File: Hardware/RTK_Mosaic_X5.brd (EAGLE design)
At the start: 151.8 x 101.6 mm, 299 parts, among them J2 MAGJACK-POE, J3 MICRO-SD-PUSH-PUSH-EXT-PIN, J4 Vertical Qwiic Connector, J9 MAGJACK-POE, U1 ESP32-WROVER-IE, U10 POE_PSU-DP990X, U17 URB2405YMD, U2 CH340C, U3 XC6222B331MR-G, U4 TXS0108, U5 TXS0108, U6 XC6222B331MR-G

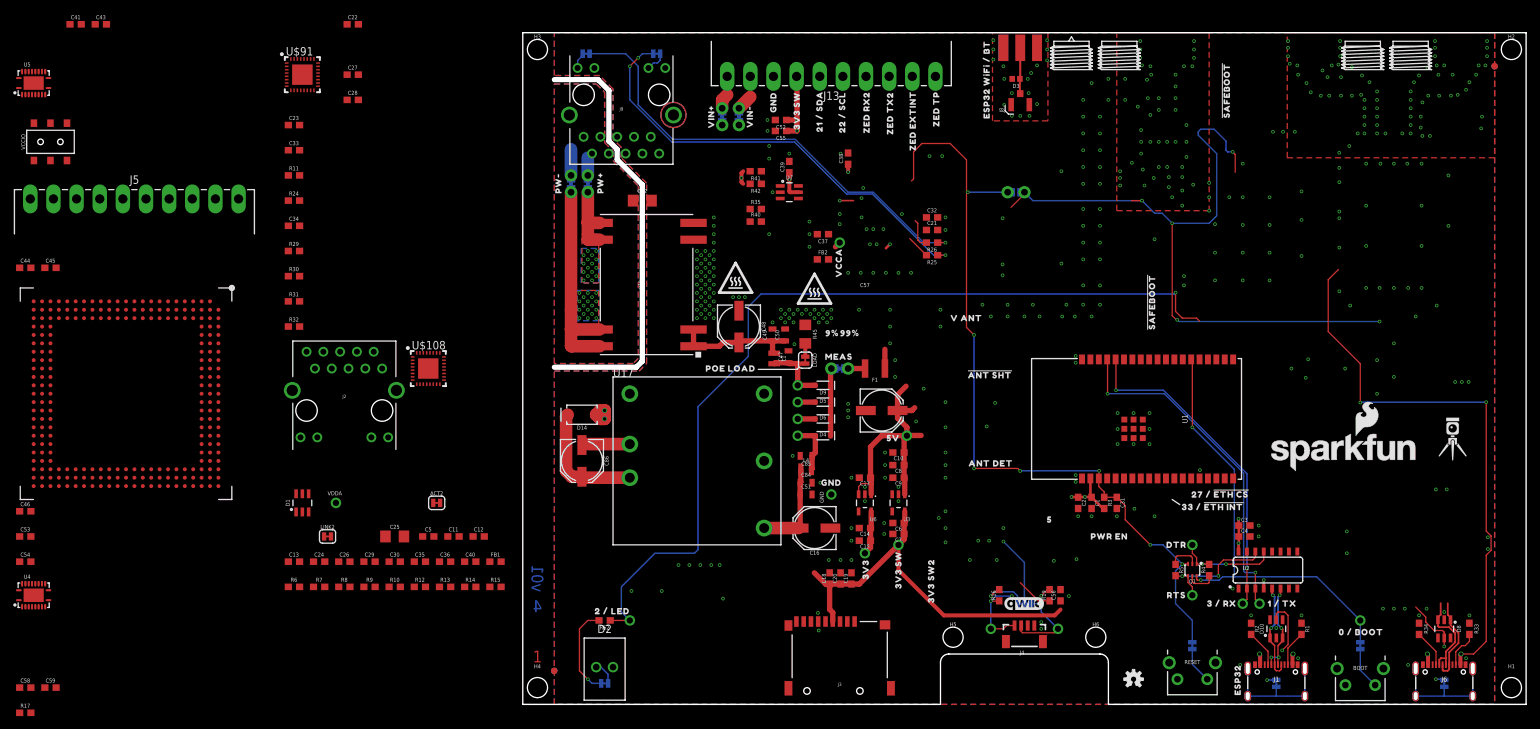
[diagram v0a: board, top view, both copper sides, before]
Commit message: Ready for airwire review
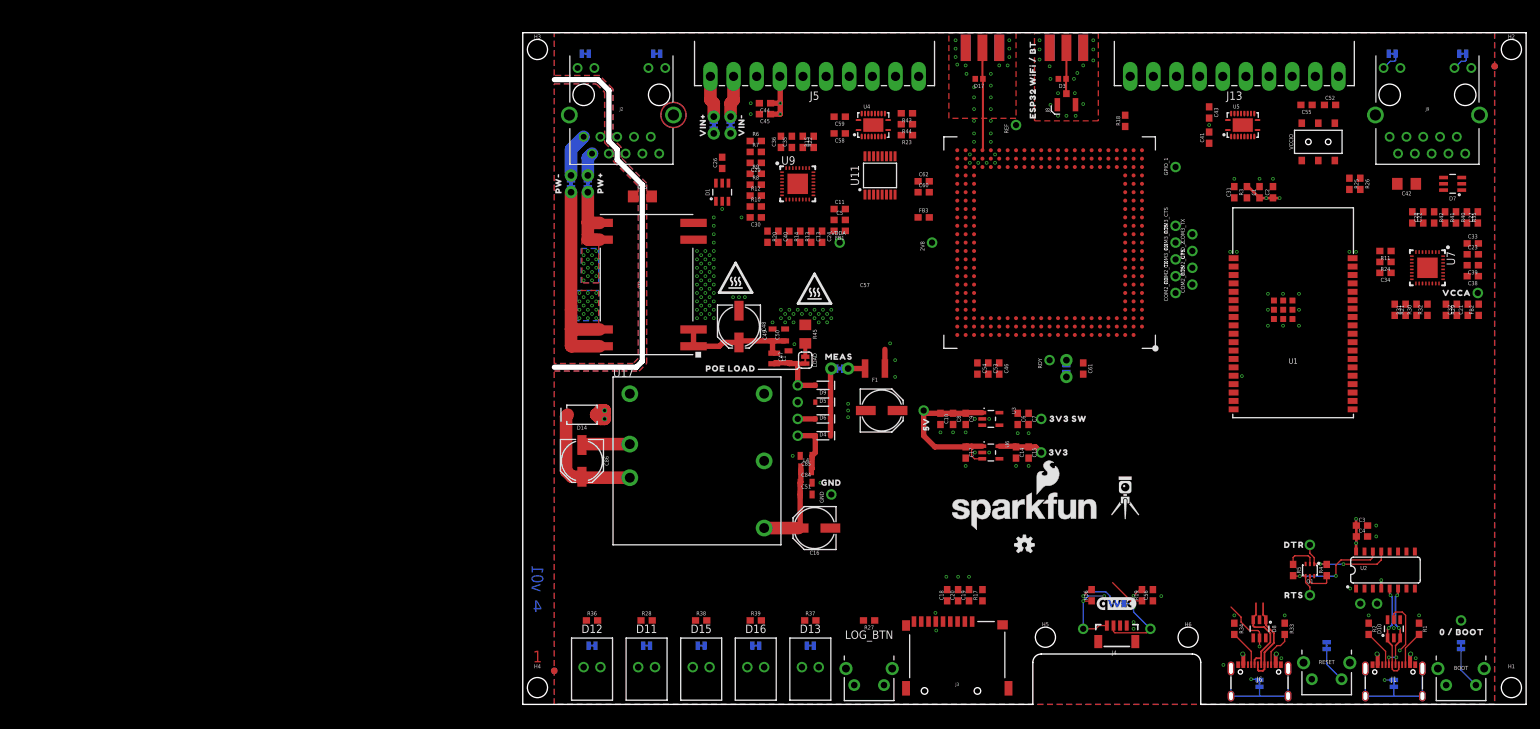
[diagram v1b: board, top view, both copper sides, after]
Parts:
- removed C12, C37: 0.1uF, SparkFun-Capacitors:0603
- removed D2: LED-RIGHT-ANGLE-PTH-GREEN, SparkFun-LED:CBI-RIGHT-ANGLE-PTH
- removed GNSS_RESET: JUMPER-COMBO_2_NO, SparkFun-Jumpers:COMBO-JUMPER_2_NO
- removed LED: JUMPER-SMT_2_NC_TRACE_SILK, SparkFun-Jumpers:SMT-JUMPER_2_NC_TRACE_SILK
- removed R62: 470, SparkFun-Resistors:0603
- removed TP_LED: TEST-POINTPOGO_PTH, SparkFun-Connectors:1X01_NO_SILK
- removed U$100, U$35: (no value), output:3_#_RX20
- removed U$101: (no value), output:19_#_POCI19
- removed U$102: (no value), output:18_#_SCK6
- removed U$104, U$47: (no value), output:99#2230
- removed U$105, U$49: (no value), output:V_ANT2229
- removed U$106, U$44: (no value), output:9#2230
- removed U$108, U$91: KSZ8041NL, Septentrio_Mosaic:MLF55Q-32LD
- removed U$109, U$27: (no value), output:33_#_#ETH_INT#0
- removed U$11: (no value), output:ZED_TX1
- removed U$111, U$29: (no value), output:27_#_#ETH_CS#0
- removed U$12, U$41, U$8, U$93: (no value), output:#SAFEBOOT#2226
- removed U$13: (no value), output:ZED_RX0
- removed U$14: (no value), output:NEO_TX2
- removed U$141, U$80: (no value), output:PWR_EN2233
- removed U$15: (no value), output:NEO_RX3
- removed U$154: (no value), output:#GNSS_RESET#0
- removed U$16: (no value), output:GND2
- removed U$17, U$65: (no value), output:3V3_SW20
- removed U$19: (no value), output:12_#_SDA20
- removed U$20: (no value), output:15_#_SCL213
- removed U$22, U$23: (no value), output:3V3_SW3
- removed U$25, U$26: (no value), output:21_#_SDA4
- removed U$28, U$30: (no value), output:22_#_SCL22
- removed U$31, U$32: (no value), output:ZED_RX223
- removed U$33, U$36: (no value), output:ZED_TX2224
- removed U$34, U$99: (no value), output:1_#_TX20
- removed U$37, U$38: (no value), output:ZED_EXTINT2225
- removed U$39, U$40: (no value), output:ZED_TP2226
- removed U$42, U$94: (no value), output:ANT_DET2227
- removed U$43, U$95: (no value), output:#ANT_SHT#2228
- removed U$48: (no value), output:#I�C#0
- removed U$57, U$66: (no value), output:2_#_LED0
- removed U$58: (no value), output:#LED#2234
- removed U$64: (no value), output:36_#_SD_DET0
- removed U$67: (no value), output:#PMODE0#0
- removed U$68: (no value), output:#PMODE1#1
- removed U$69: (no value), output:#PMODE2#2
- removed U$73, U$75: (no value), output:50
- removed U$78: (no value), output:ESP320
- removed U$79: (no value), output:UART14
- removed U$89: (no value), output:4_#_#SD_CS#15
- removed U$98: (no value), output:23_#_PICO23
- added 2V8, COM2_CTS, COM2_RTS, COM2_RX, COM2_TX, COM3_CTS, COM3_RTS, COM3_RX, COM3_TX, GPIO_1, GPIO_2, RDY, REF: TEST-POINTPOGO_PTH, SparkFun-Connectors:1X01_NO_SILK
- added BT, LOG, PVT, RTK, WIFI: JUMPER-SMT_2_NC_TRACE_SILK, SparkFun-Jumpers:SMT-JUMPER_2_NC_TRACE_SILK
- added C60, C61: 2.2uF, SparkFun-Capacitors:0603
- added C62: 0.1uF, SparkFun-Capacitors:0603
- added D11: LED-RIGHT-ANGLE-PTH-AMBER, SparkFun-LED:CBI-RIGHT-ANGLE-PTH
- added D12, D15, D16: LED-RIGHT-ANGLE-PTH-BLUE, SparkFun-LED:CBI-RIGHT-ANGLE-PTH
- added D13: LED-RIGHT-ANGLE-PTH-GREEN, SparkFun-LED:CBI-RIGHT-ANGLE-PTH
- added D17: PESD0402, SparkFun-DiscreteSemi:0402
- added FB3: 470Ω, SparkFun-Coils:0603
- added LOG_BTN: MOMENTARY-SWITCH-SPST-PTH-RIGHT-ANGLE-8-020, SparkFun-Switches:TACTILE_SWITCH_PTH_RA_8-020
- added MOSAIC_RF: ANTENNA-SMA-GROUNDEDEDGE_SMA, SparkFun-RF:SMA-EDGE
- added MOSAIC_RST: JUMPER-COMBO_2_NO, SparkFun-Jumpers:COMBO-JUMPER_2_NO
- added R18, R22, R23, R43, R44: 10k, SparkFun-Resistors:0603
- added R20, R21: 4.7k, SparkFun-Resistors:0603
- added R27, R28, R36, R37, R38, R39: 1k, SparkFun-Resistors:0603
- added U11: SN74AVC4T774PW, SparkFun-IC-Comms:SOP65P640X120-16N
- added U7, U9: KSZ8041NL, Septentrio_Mosaic:MLF55Q-32LD
- added U8: MOSAIC-X5X5, Septentrio_Mosaic:MOSAIC_LGA
- U$2: value MOSAIC-X5X5 -> (none); device Septentrio_Mosaic:MOSAIC_LGA -> output:#ACT#0
- U$4: device output:#I�C#0 -> output:#LINK#1
- moved VCCIO 191.8 mm to (120.7, 85.1)
- moved U5 183.0 mm to (109.2, 87.6)
- moved C23 179.4 mm to (144.0, 68.1)
- moved C33 178.9 mm to (144.0, 69.7)
- moved R29 174.5 mm to (140.0, 59.7), turned to 270 degrees
- moved C41 172.3 mm to (104.1, 85.7), turned to 90 degrees
- moved C27 171.5 mm to (144.8, 73.7), turned to 90 degrees
- moved R32 171.5 mm to (137.2, 59.7), turned to 90 degrees
- moved R30 169.9 mm to (135.5, 59.7), turned to 90 degrees
- moved C43 168.2 mm to (104.1, 89.5), turned to 270 degrees
- moved R31 168.2 mm to (133.9, 59.7), turned to 90 degrees
- moved R11 165.5 mm to (130.8, 68.6), turned to 180 degrees
- moved R24 165.4 mm to (130.8, 66.9), turned to 180 degrees
- moved C34 165.3 mm to (130.8, 65.3), turned to 180 degrees
- moved C22 162.9 mm to (134.9, 73.7), turned to 270 degrees
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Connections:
- removed net ESP2/LED: R62.1, TP_LED.1
- removed net GNSS_!RESET!: GNSS_RESET.1, GNSS_RESET.3
- removed net N$45: D2.A, LED.1
- removed net N$7: LED.2, R62.2
- removed net SD_DAT0: J3.7
- new net 1.8V: C60.1, C62.1, R18.2, U11.16, U11.6, U11.7, U11.8, U8.AC4
- new net 2V8: 2V8.1, U8.M23, U8.N23
- new net COM2_CTS: COM2_CTS.1, U8.J1
- new net COM2_RTS: COM2_RTS.1, U8.G1
- new net COM2_RX: COM2_RX.1, U8.F1
- new net COM2_TX: COM2_TX.1, U8.H1
- new net COM3_CTS: COM3_CTS.1, U8.N1
- new net COM3_RTS: COM3_RTS.1, U8.L1
- new net COM3_RX: COM3_RX.1, U8.K1
- new net COM3_TX: COM3_TX.1, U8.M1
- new net GPIO_1: GPIO_1.1, U8.AA4
- new net GPIO_2: GPIO_2.1, U8.L3
- new net LED_PVT: R38.1, U8.A14
- new net LED_RTK: R39.1, U8.M3
- new net LOG_LED: R37.1, U8.B2
- new net MOSAIC_!RST!: MOSAIC_RST.1, MOSAIC_RST.3, U8.A11
- new net MOSAIC_EVENTA_1V8: U11.3, U8.AC6
- new net MOSAIC_EVENTB_1V8: U11.4, U8.AC7
- new net MOSAIC_PPSO_1V8: U11.5, U8.AC8
- new net MOSAIC_RF: D17.1, MOSAIC_RF.SIG, U8.AC20
- new net N$11: LOG_BTN.2, R27.1
- new net N$16: LOG.2, R37.2
- new net N$17: D13.A, LOG.1
- new net N$18: D11.A, WIFI.1
- new net N$22: BT.1, D12.A
- new net N$26: BT.2, R36.2
- new net N$32: R28.2, WIFI.2
- new net N$35: D15.A, PVT.1
- new net N$36: D16.A, RTK.1
- new net N$37: R39.2, RTK.2
- new net N$38: PVT.2, R38.2
- new net N$6: FB3.2, U8.P23, U8.R23
- new net N$9: R18.1, U8.AC3
- new net RDY: RDY.1, U8.A12
- new net REF: REF.1, U8.AC16, U8.AC17
- net !RESET!: now also MOSAIC_RST.2, MOSAIC_RST.4; no longer GNSS_RESET.2, GNSS_RESET.4
- net 3.3V: now also R21.2, U7.17; no longer U$91.17
- net 3.3V_SW: now also R20.2, U11.15, U8.A18, U8.A19, U8.A20, U8.B18, U8.B19, U8.B20, U8.B8, U8.C18, U8.C19, U8.C20, U9.17; no longer U$108.17, U$2.A18, U$2.A19, U$2.A20, U$2.B18, U$2.B19, U$2.B20, U$2.B8, U$2.C18, U$2.C19, U$2.C20
- net 5V: now also C61.1, FB3.1, U8.A8; no longer U$2.A8, U$2.P23, U$2.R23
- net ACT_ESP32: now also U7.31; no longer U$91.31
- net ACT_MOSAIC: now also U9.31; no longer U$108.31
- net D+_MOSAIC: now also U8.A5; no longer U$2.A5
- net D-_MOSAIC: now also U8.A6; no longer U$2.A6
- net ESP0/!BOOT!: now also U7.9; no longer U$91.9
- net ESP12_LED_WIFI: now also R28.1
- net ESP15_LED_BT: now also R36.1
- net ESP18_MDIO: now also R21.1, U7.11; no longer U$91.11
- net ESP19_TXD0: now also U7.24; no longer U$91.24
- net ESP21_TXEN: now also U7.23; no longer U$91.23
- net ESP22_TXD1: now also U7.25; no longer U$91.25
- net ESP23_MDC: now also U7.12; no longer U$91.12
- net ESP2_COM4_RX: now also U8.D3; no longer U$2.D3
- net ESP32_TX: now also U5.3; no longer U5.1
- net ESP32_TX_IO: now also U5.18; no longer U5.20
- net ESP33_RTS: now also U5.4; no longer U5.3
- net ESP33_RTS_IO: now also U5.17; no longer U5.18
- net ESP34_RX: now also U5.1; no longer U5.4
- net ESP34_RX_IO: now also U5.20; no longer U5.17
- net ESP4_COM4_TX: now also U8.E3; no longer U$2.E3
- net ESP5_ERST: now also U7.32; no longer U$91.32
- net ETHER_!RST!: now also R22.2, U8.F2, U9.32; no longer U$2.F2
- net ETHER_CLK: now also U8.AA2, U9.9; no longer U$108.9, U$2.AA2
- net ETHER_CRSDV: now also U8.N2, U9.18; no longer U$108.18, U$2.N2
- net ETHER_MDC: now also U8.V2, U9.12; no longer U$108.12, U$2.V2
- net ETHER_MDIO: now also R20.1, U8.W2, U9.11; no longer U$108.11, U$2.W2
- net ETHER_RXD0: now also U8.R2, U9.16; no longer U$108.16, U$2.R2
- net ETHER_RXD1: now also U8.T2, U9.15; no longer U$108.15, U$2.T2
- net ETHER_RXER: now also U8.M2, U9.20; no longer U$108.20, U$2.M2
- net ETHER_TXD0: now also U8.J2, U9.24; no longer U$108.24, U$2.J2
- net ETHER_TXD1: now also U8.H2, U9.25; no longer U$108.25, U$2.H2
- net ETHER_TXEN: now also U8.L2, U9.23; no longer U$108.23, U$2.L2
- net GND: now also C60.2, C61.2, C62.2, D11.C, D12.C, D13.C, D15.C, D16.C, D17.2, LOG_BTN.1, MOSAIC_RF.GND@0, MOSAIC_RF.GND@1, MOSAIC_RF.GND@2, MOSAIC_RF.GND@3, R22.1, R43.1, R44.1, U11.1, U11.10, U11.2, U11.9, U7.1, U7.GND, U8.A15, U8.A16, U8.A17, U8.A21, U8.A22, U8.A23, U8.A3, U8.A4, U8.A7, U8.AA13, U8.AA14, U8.AA15, U8.AA16, U8.AA17, U8.AA18, U8.AA19, U8.AA20, U8.AA21, U8.AA22, U8.AA23, U8.AB13, U8.AB14, U8.AB15, U8.AB16, U8.AB17, U8.AB18, U8.AB19, U8.AB2, U8.AB20, U8.AB21, U8.AB22, U8.AB23, U8.AB3, U8.AB4, U8.AB5, U8.AB6, U8.AB7, U8.AB8, U8.AC13, U8.AC15, U8.AC18, U8.AC19, U8.AC21, U8.AC22, U8.AC23, U8.B13, U8.B17, U8.B21, U8.B4, U8.B5, U8.B6, U8.B7, U8.C15, U8.C16, U8.C17, U8.C23, U8.C4, U8.C7, U8.D2, U8.D21, U8.D22, U8.D23, U8.E2, U8.E21, U8.E22, U8.E23, U8.F21, U8.F22, U8.F23, U8.G2, U8.G21, U8.G23, U8.H21, U8.H22, U8.H23, U8.J21, U8.J22, U8.J23, U8.K2, U8.K21, U8.K22, U8.K23, U8.L21, U8.L22, U8.L23, U8.M21, U8.M22, U8.N21, U8.N22, U8.P1, U8.P2, U8.P21, U8.P22, U8.P3, U8.R21, U8.R22, U8.R3, U8.T21, U8.T22, U8.T23, U8.U2, U8.U21, U8.U22, U8.U23, U8.V21, U8.V22, U8.V23, U8.W21, U8.W22, U8.W23, U8.Y2, U8.Y21, U8.Y22, U8.Y23, U9.1, U9.GND; no longer C12.2, C37.2, D2.C, U$108.1, U$108.GND, U$2.A15, U$2.A16, U$2.A17, U$2.A21, U$2.A22, U$2.A23, U$2.A4, U$2.A7, U$2.AA13, U$2.AA14, U$2.AA15, U$2.AA16, U$2.AA17, U$2.AA18, U$2.AA19, U$2.AA20, U$2.AA21, U$2.AA22, U$2.AA23, U$2.AB13, U$2.AB14, U$2.AB15, U$2.AB16, U$2.AB17, U$2.AB18, U$2.AB19, U$2.AB2, U$2.AB20, U$2.AB21, U$2.AB22, U$2.AB23, U$2.AB3, U$2.AB4, U$2.AB5, U$2.AB6, U$2.AB7, U$2.AB8, U$2.AC13, U$2.AC15, U$2.AC18, U$2.AC19, U$2.AC21, U$2.AC22, U$2.AC23, U$2.B13, U$2.B17, U$2.B21, U$2.B4, U$2.B5, U$2.B6, U$2.B7, U$2.C15, U$2.C16, U$2.C17, U$2.C23, U$2.C4, U$2.C7, U$2.D2, U$2.D21, U$2.D22, U$2.D23, U$2.E2, U$2.E21, U$2.E22, U$2.E23, U$2.F21, U$2.F22, U$2.F23, U$2.G2, U$2.G21, U$2.G23, U$2.H21, U$2.H22, U$2.H23, U$2.J21, U$2.J22, U$2.J23, U$2.K2, U$2.K21, U$2.K22, U$2.K23, U$2.L21, U$2.L22, U$2.L23, U$2.M21, U$2.M22, U$2.N21, U$2.N22, U$2.P1, U$2.P2, U$2.P21, U$2.P22, U$2.P3, U$2.R21, U$2.R22, U$2.R3, U$2.T21, U$2.T22, U$2.T23, U$2.U2, U$2.U21, U$2.U22, U$2.U23, U$2.V21, U$2.V22, U$2.W21, U$2.W22, U$2.W23, U$2.Y2, U$2.Y21, U$2.Y22, U$2.Y23, U$91.1, U$91.GND
- net LINK_ESP32: now also U7.30; no longer U$91.30
- net LINK_MOSAIC: now also U9.30; no longer U$108.30
- net MOSAIC_CTS: now also U8.E1; no longer U$2.E1
- net MOSAIC_EVENTA: now also U11.14; no longer U$2.AC6
- net MOSAIC_EVENTA_IO: now also R43.2
- net MOSAIC_EVENTB: now also U11.13; no longer U$2.AC7
- net MOSAIC_EVENTB_IO: now also R44.2
- net MOSAIC_LOG_BTN: now also U8.K3; no longer U$2.K3
- net MOSAIC_LOG_BTN_IO: now also R23.2, R27.2
- net MOSAIC_PPSO: now also U11.12; no longer U$2.AC8
- net MOSAIC_RTS: now also U8.C1; no longer U$2.C1
- net MOSAIC_RX: now also U8.B1; no longer U$2.B1
- net MOSAIC_TX: now also U8.D1; no longer U$2.D1
- net N$146: now also U9.2; no longer U$108.2
- net N$147: now also U9.10; no longer U$108.10
- net N$148: now also U9.28; no longer U$108.28
- net N$23: now also U7.2; no longer U$91.2
- net N$24: now also U7.10; no longer U$91.10
- net N$25: now also U7.28; no longer U$91.28
- net N$30: now also U7.16; no longer U$91.16
- net N$31: now also U7.15; no longer U$91.15
- net N$39: now also U7.18; no longer U$91.18
- net RD+_ESP32: now also U7.5; no longer U$91.5
- net RD+_MOSAIC: now also D1.1, U9.5; no longer D1.4, U$108.5
- net RD-_ESP32: now also D7.6, U7.4; no longer D7.3, U$91.4
- net RD-_MOSAIC: now also U9.4; no longer U$108.4
- net SD_CLK: now also U8.AA1; no longer U$2.AA1
- net SD_CMD: now also U8.AB1; no longer U$2.AB1
- net SD_DATA: now also J3.7, U8.Y1; no longer U$2.Y1
- net TD+_ESP32: now also D7.3, U7.7; no longer D7.6, U$91.7
- net TD+_MOSAIC: now also U9.7; no longer U$108.7
- net TD-_ESP32: now also U7.6; no longer U$91.6
- net TD-_MOSAIC: now also D1.4, U9.6; no longer D1.1, U$108.6
- net VCCA: now also U7.3; no longer C37.1, U$91.3
- net VCCIO: now also R23.1
- net VDDA: now also U9.3; no longer C12.1, U$108.3
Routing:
- net V_USB_2: track 240.5 -> 23.0 mm, vias 5 -> 3
- net ESP2/LED: track 135.0 -> 0.00 mm, vias 1 -> 0
- net !RESET!: track 123.0 -> 0.00 mm, vias 7 -> 0
- net V_USB: track 141.6 -> 21.6 mm
- net GNSS_!RESET!: track 107.4 -> 0.00 mm, vias 5 -> 0
- net 3.3V: track 108.2 -> 31.5 mm, vias 10 -> 5
- net N$12: track 70.3 -> 0.00 mm, vias 1 -> 0
- net N$21: track 68.1 -> 0.00 mm, vias 3 -> 0
- net ESP0/!BOOT!: track 67.1 -> 0.00 mm, vias 2 -> 0
- net 3.3V_SW: track 58.7 -> 0.00 mm
- net CH340-RXI: track 52.4 -> 0.00 mm, vias 2 -> 0
- net CH340-TXO: track 49.6 -> 0.00 mm, vias 2 -> 0
- net VCCA: track 49.5 -> 0.00 mm, vias 10 -> 0
- net MOSAIC_RF: track 0.00 -> 15.6 mm
- net N$7: track 13.9 -> 0.00 mm, vias 1 -> 0
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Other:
- outline, holes or cut-outs redrawn
- board text added: "Controlled Impedance: JLC7628 Material: TG155 4-Layers Thickness: 1.6mm Outer Copper: 1oz Inner Copper: 0.5oz Finish: ENIG Red Solder Resist White Silkscreen No clean process"
- board text removed: "Controlled Impedance: JLC7628 Material: TG155 4-Layers Thickness: 1.6mm Outer Copper: 1oz Inner Copper: 0.5oz Finish: HASL Lead Free Red Solder Resist White Silkscreen"

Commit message: Silk added. Layer 15 polygon is now GND.
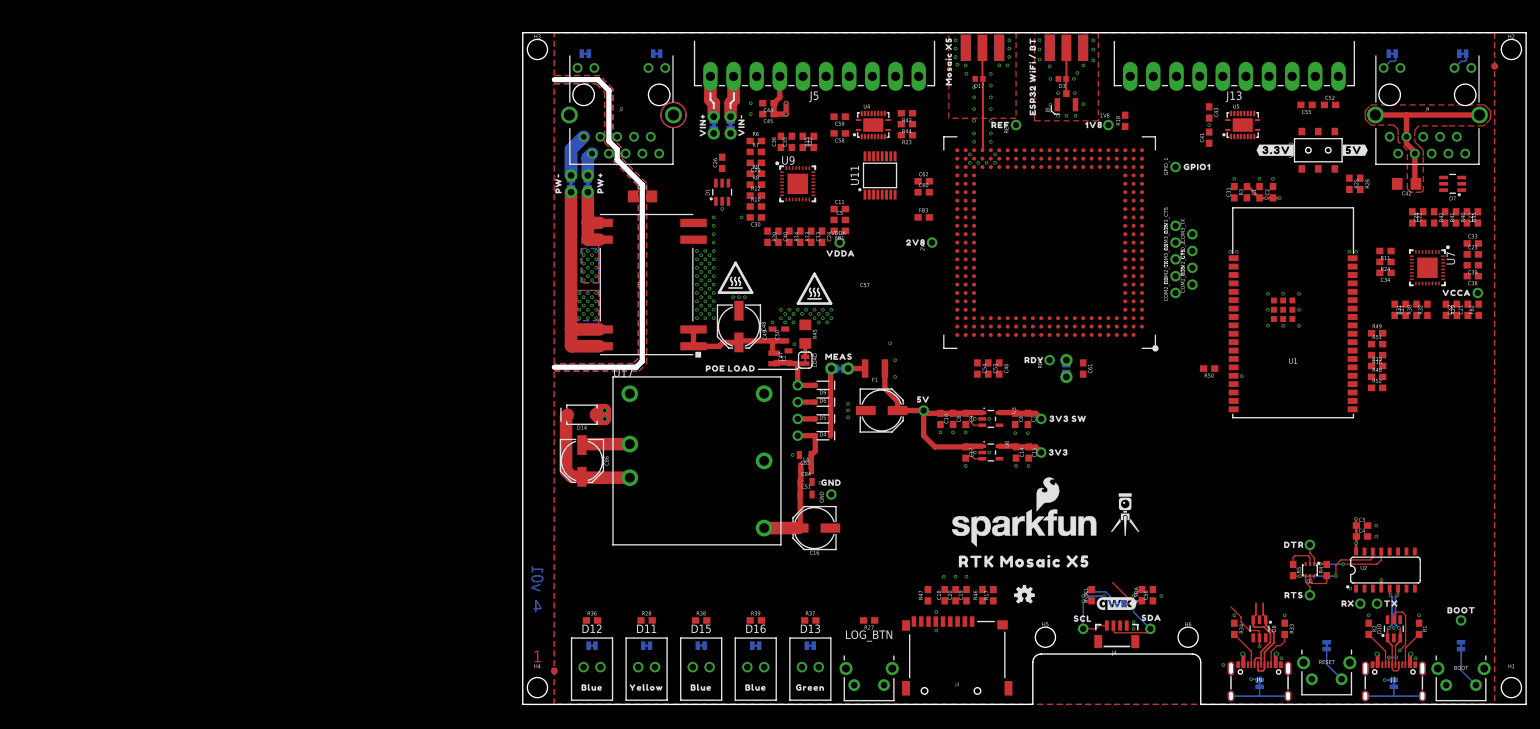
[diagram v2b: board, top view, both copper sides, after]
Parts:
- removed U$148: (no value), output:RESET0
- removed U$149: (no value), output:0_#_BOOT0
- added 1V8: TEST-POINTPOGO_PTH, SparkFun-Connectors:1X01_NO_SILK
- added R46, R47, R48, R49, R50: 10k, SparkFun-Resistors:0603
- added R51, R52: 0, SparkFun-Resistors:0603
- added R_SCL, R_SDA: 2.2k, SparkFun-Resistors:0603
- added U$100: (no value), output:MOSAIC_X50
- added U$101, U$102: (no value), output:1V80
- added U$103, U$105, U$106: (no value), output:BLUE0
- added U$104: (no value), output:YELLOW1
- added U$108: (no value), output:GREEN2
- added U$11: (no value), output:#LOG#4
- added U$12: (no value), output:#PVT#2
- added U$13: (no value), output:#RTK#3
- added U$14: (no value), output:#WIFI#1
- added U$15: (no value), output:#BOOT#6
- added U$16: (no value), output:#_______________MOSAIC_X5_______________#8
- added U$17, U$31: (no value), output:#RX#2
- added U$19, U$29: (no value), output:#RTS#4
- added U$20, U$30: (no value), output:#CTS#5
- added U$22: (no value), output:#EVENT_A#6
- added U$23: (no value), output:#EVENT_B#7
- added U$25, U$28: (no value), output:#GND#0
- added U$26, U$27: (no value), output:#VCCIO#1
- added U$32: (no value), output:#TX#3
- added U$33: (no value), output:#PPSO#11
- added U$34: (no value), output:#LOG_BTN#33
- added U$35: (no value), output:#SCL#10
- added U$36: (no value), output:#SDA#9
- added U$37: (no value), output:#MOSAIC#8
- added U$38: (no value), output:#___________________ESP32___________________#34
- added U$39: (no value), output:#3#3V#6
- added U$40: (no value), output:#5V#0
- added U$41, U$42: (no value), output:2V8220
- added U$43, U$44: (no value), output:BOOT2
- added U$47: (no value), output:COM2_CTS219
- added U$48: (no value), output:COM2_RTS219
- added U$49: (no value), output:COM2_RX219
- added U$54: (no value), output:COM2_TX219
- added U$57: (no value), output:COM3_CTS18
- added U$58: (no value), output:COM3_RTS18
- added U$64: (no value), output:COM3_RX219
- added U$65: (no value), output:COM3_TX18
- added U$66, U$67: (no value), output:GPIO17
- added U$68: (no value), output:GPIO218
- added U$69, U$99: (no value), output:RTK_MOSAIC_X50
- added U$73: (no value), output:MOSAIC_#RST#6
- added U$75, U$78: (no value), output:RDY5
- added U$79, U$80: (no value), output:REF219
- added U$8: (no value), output:#BT#0
- added U$89, U$90: (no value), output:RX0
- added U$91, U$92: (no value), output:SCL3
- added U$93, U$94: (no value), output:SDA4
- added U$95, U$96: (no value), output:TX1
- added U$97, U$98: (no value), output:VDDA220
- R16: value 2.2k -> 10k
- R19: value 2.2k -> 1k
- U$18: device output:GND2 -> output:#TX#3
- U$7: device output:0_#_BOOT0 -> output:##RESET##5
- moved R16 56.4 mm to (129.5, 52.8), turned to 180 degrees
- moved R19 49.7 mm to (129.5, 51.2), turned to 0 degrees
- moved U$7 19.8 mm to (122.7, 8.89), flipped to the bottom
- moved U$18 10.8 mm to (46.4, 89.3)
- moved LOGO4 7.62 mm to (76.2, 16.5)
- moved U$86 5.90 mm to (59.1, 46.1), turned to 0 degrees
- moved U$153 3.81 mm to (61.0, 27.6)
- moved D5 2.54 mm to (45.7, 43.2)
- moved D6 2.54 mm to (45.7, 45.7)
- moved LOGO5 2.54 mm to (76.2, 26.7)
- moved LOGO6 2.54 mm to (79.8, 31.8)
- moved LOGO7 2.54 mm to (76.2, 26.7)
- moved LOGO8 2.54 mm to (72.6, 31.8)
- moved U$152 2.54 mm to (91.4, 28.7)
- moved U$82 2.54 mm to (42.2, 43.2)
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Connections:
- net N$3 renamed SD_DAT3
- removed net ESP0/!BOOT!: BOOT_SW.1, Q1.6, TP_BOOT.1, U1.25, U7.9
- removed net ESP2_COM4_RX: U1.24, U8.D3
- removed net ESP4_COM4_TX: U1.26, U8.E3
- new net !BOOT!: BOOT_SW.1, Q1.6, R16.1, R19.2, TP_BOOT.1
- new net COM4_RX: R52.2, U8.D3
- new net COM4_TX: R51.2, U8.E3
- new net ESP2_TX: R48.1, R52.1, U1.24
- new net ESP4_RX: R51.1, U1.26
- new net ESP_REFCLK: R19.1, U1.25, U7.9
- net 1.8V: now also 1V8.1
- net 3.3V: now also R16.2, R49.2
- net 3.3V_SW: now also R22.1, R46.2, R47.2
- net ESP12_LED_WIFI: now also R50.1
- net ESP14_SCL: now also R_SCL.1; no longer R16.1
- net ESP15_SDA: now also R_SDA.1; no longer R19.1
- net ESP5_ERST: now also R49.1
- net GND: now also R48.2, R50.2; no longer R22.1
- net N$14: now also R_SCL.2; no longer R16.2
- net N$15: now also R_SDA.2; no longer R19.2
- net SD_CMD: now also R46.1
- net SD_DATA: now also R47.1
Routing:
- net GND-ISO: track 0.00 -> 26.7 mm
- net 5V: track 28.7 -> 40.2 mm
- net 3.3V_SW: track 0.00 -> 6.71 mm
- net V_USB: track 21.6 -> 24.3 mm
- net VCCIO: track 8.64 -> 9.56 mm
- removed copper zone on layer 15, net 3.3V_SW

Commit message: Routed
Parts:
- moved R26 8.03 mm to (133.2, 73.7)
- moved R25 8.03 mm to (131.6, 73.7)
- moved C5 3.81 mm to (48.3, 77.1)
- moved U$152 3.81 mm to (91.4, 24.9)
- moved 2V8 3.81 mm to (62.2, 66.0)
- moved C11 3.81 mm to (48.3, 78.7)
- moved U$41 3.81 mm to (62.0, 66.0)
- moved U$42 3.81 mm to (57.4, 66.0)
- moved U$153 2.54 mm to (61.0, 25.0)
- moved C58 1.52 mm to (48.3, 84.8)
- moved C13 1.27 mm to (43.9, 69.5)
- moved C24 1.27 mm to (45.6, 69.5)
- moved C40 1.27 mm to (39.0, 69.5)
- moved R13 1.27 mm to (42.3, 69.5)
- moved R14 1.27 mm to (40.6, 69.5)
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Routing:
- net 3.3V: track 31.5 -> 308.0 mm, vias 5 -> 17
- net 3.3V_SW: track 6.71 -> 270.2 mm, vias 0 -> 11
- net MOSAIC_LOG_BTN_IO: track 0.00 -> 148.9 mm, vias 0 -> 6
- net 5V: track 40.2 -> 181.3 mm, vias 0 -> 6
- net V_USB: track 24.3 -> 165.3 mm
- net VCCIO: track 9.56 -> 129.8 mm, vias 2 -> 7
- net V_USB_2: track 23.0 -> 143.0 mm
- net ESP15_LED_BT: track 0.00 -> 119.3 mm, vias 0 -> 2
- net LED_RTK: track 0.00 -> 113.3 mm, vias 0 -> 2
- net !RESET!: track 0.00 -> 112.9 mm, vias 0 -> 4
- net ESP12_LED_WIFI: track 0.00 -> 112.0 mm, vias 0 -> 2
- net ESP15_SDA: track 17.7 -> 124.1 mm, vias 1 -> 5
- net SD_DATA: track 0.00 -> 89.1 mm, vias 0 -> 2
- net SD_CMD: track 0.00 -> 88.4 mm, vias 0 -> 2
- net ESP14_SCL: track 12.8 -> 100.4 mm, vias 2 -> 6
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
